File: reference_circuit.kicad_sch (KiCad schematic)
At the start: 14 parts, among them U11 OPA4202, U2 LM399

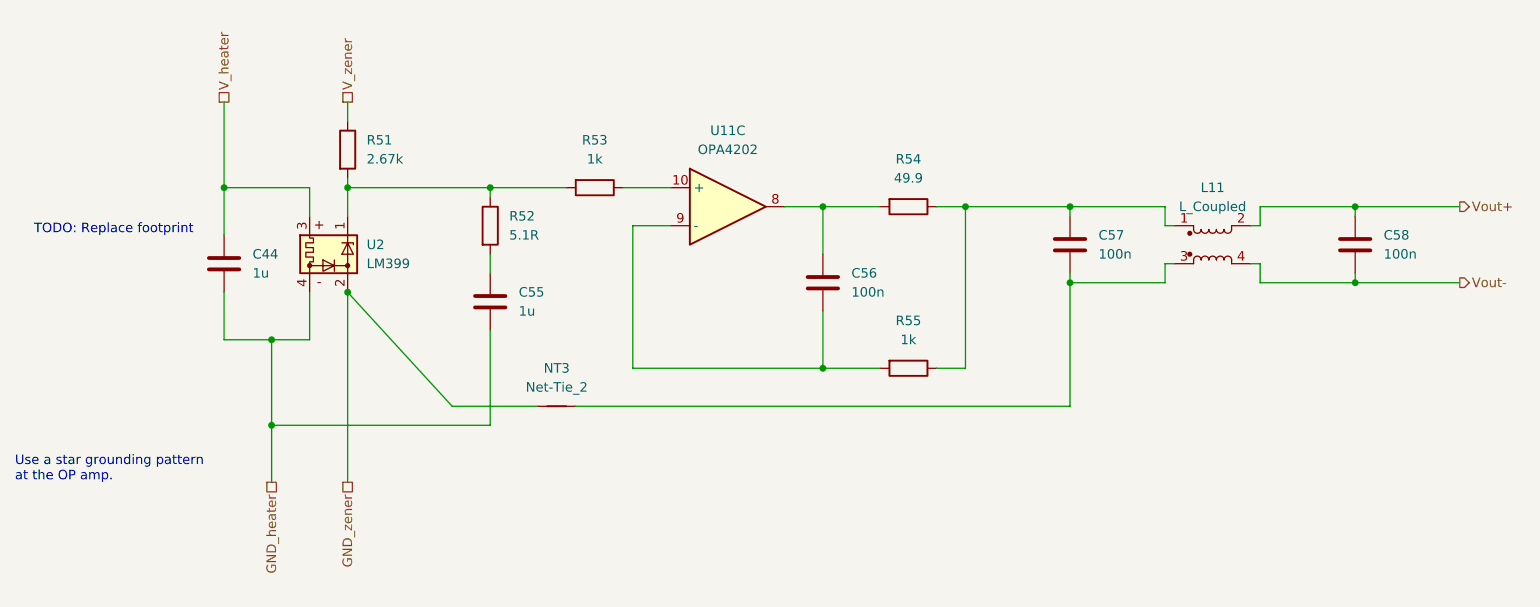
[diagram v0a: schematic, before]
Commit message: Fixed PCB date
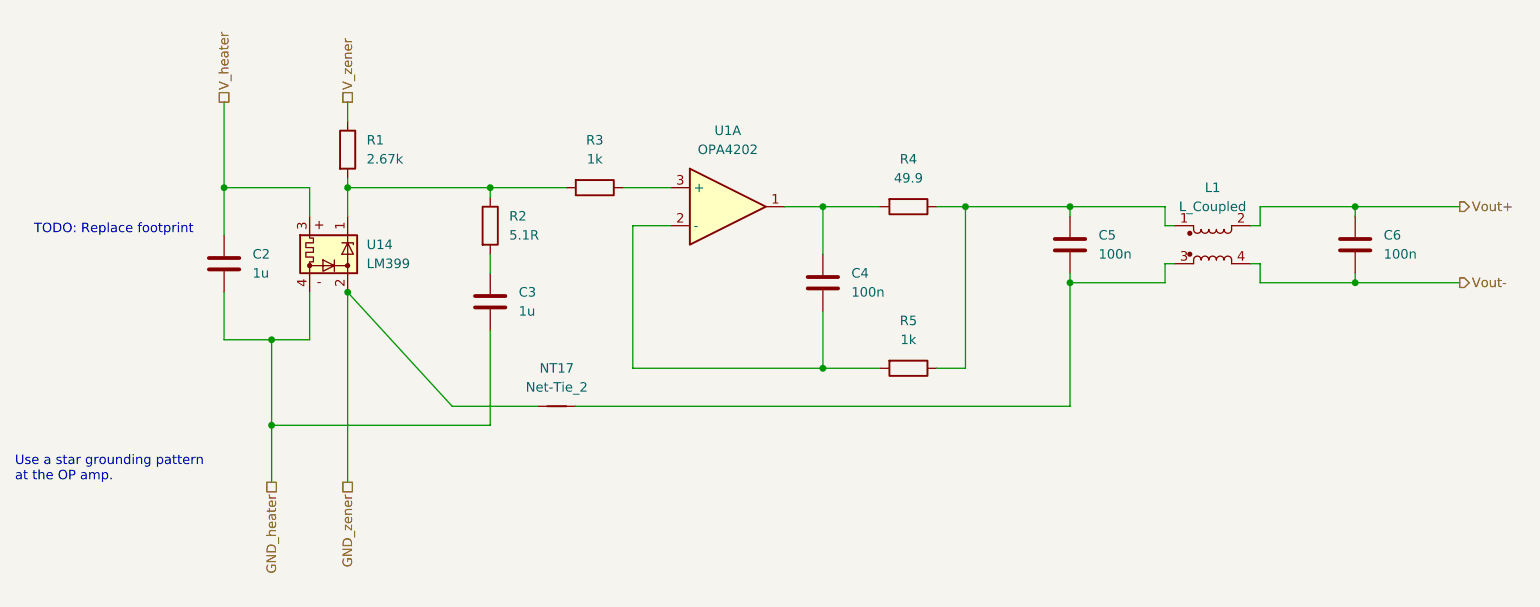
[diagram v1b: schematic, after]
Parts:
- renumbered C44 to C2, C55 to C3, C56 to C4, C57 to C5, C58 to C6, L11 to L1, NT3 to NT17, R51 to R1, R52 to R2, R53 to R3, R54 to R4, R55 to R5, U11 to U1, U2 to U14
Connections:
- net at R3.1: now also U1.3 (+); no longer U1.10 (+)
- net at C4.1, R4.2: now also U1.1; no longer U1.8
- net at C4.2, R5.2: now also U1.2 (-); no longer U1.9 (-)

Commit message: Update KiCad to version 8 (#2)
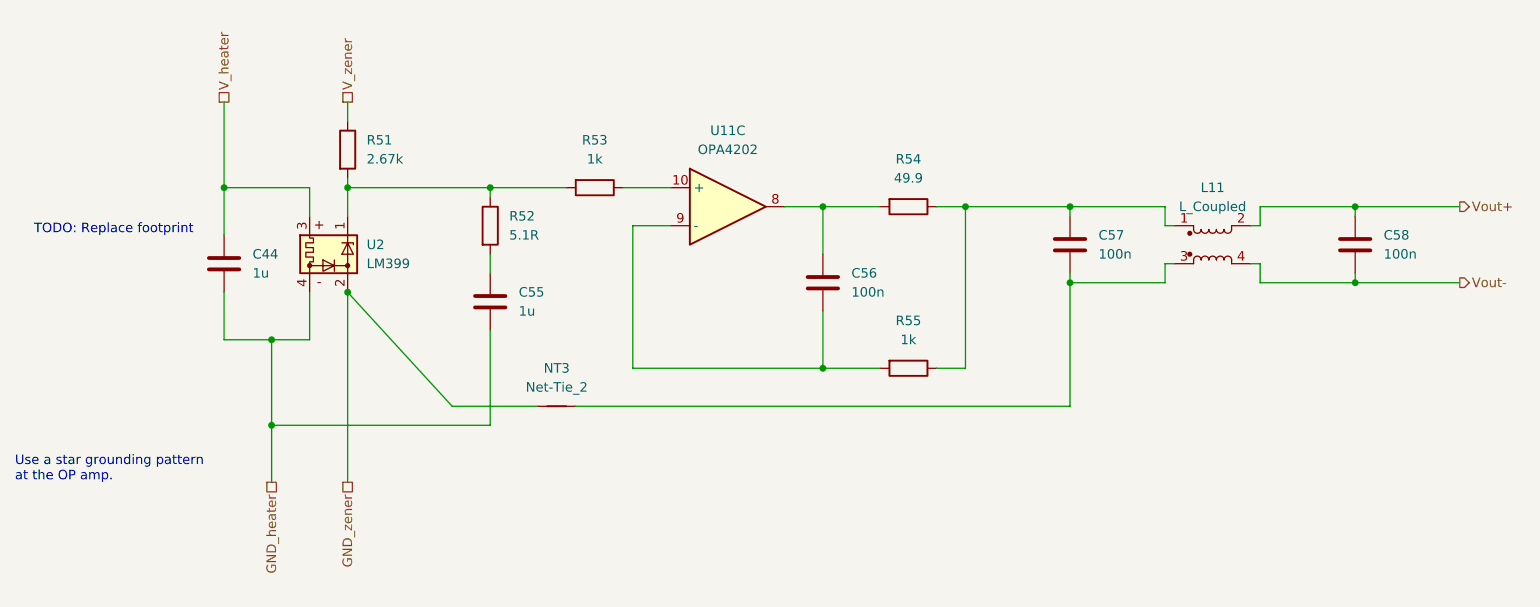
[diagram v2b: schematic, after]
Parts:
- renumbered C2 to C44, C3 to C55, C4 to C56, C5 to C57, C6 to C58, L1 to L11, NT17 to NT3, R1 to R51, R2 to R52, R3 to R53, R4 to R54, R5 to R55, U1 to U11, U14 to U2
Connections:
- net at C56.1, R54.2: now also U11.8; no longer U11.1
- net at C56.2, R55.2: now also U11.9 (-); no longer U11.2 (-)
- net at R53.1: now also U11.10 (+); no longer U11.3 (+)
